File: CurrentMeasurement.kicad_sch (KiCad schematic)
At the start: 7 parts, among them U1 DDC112U

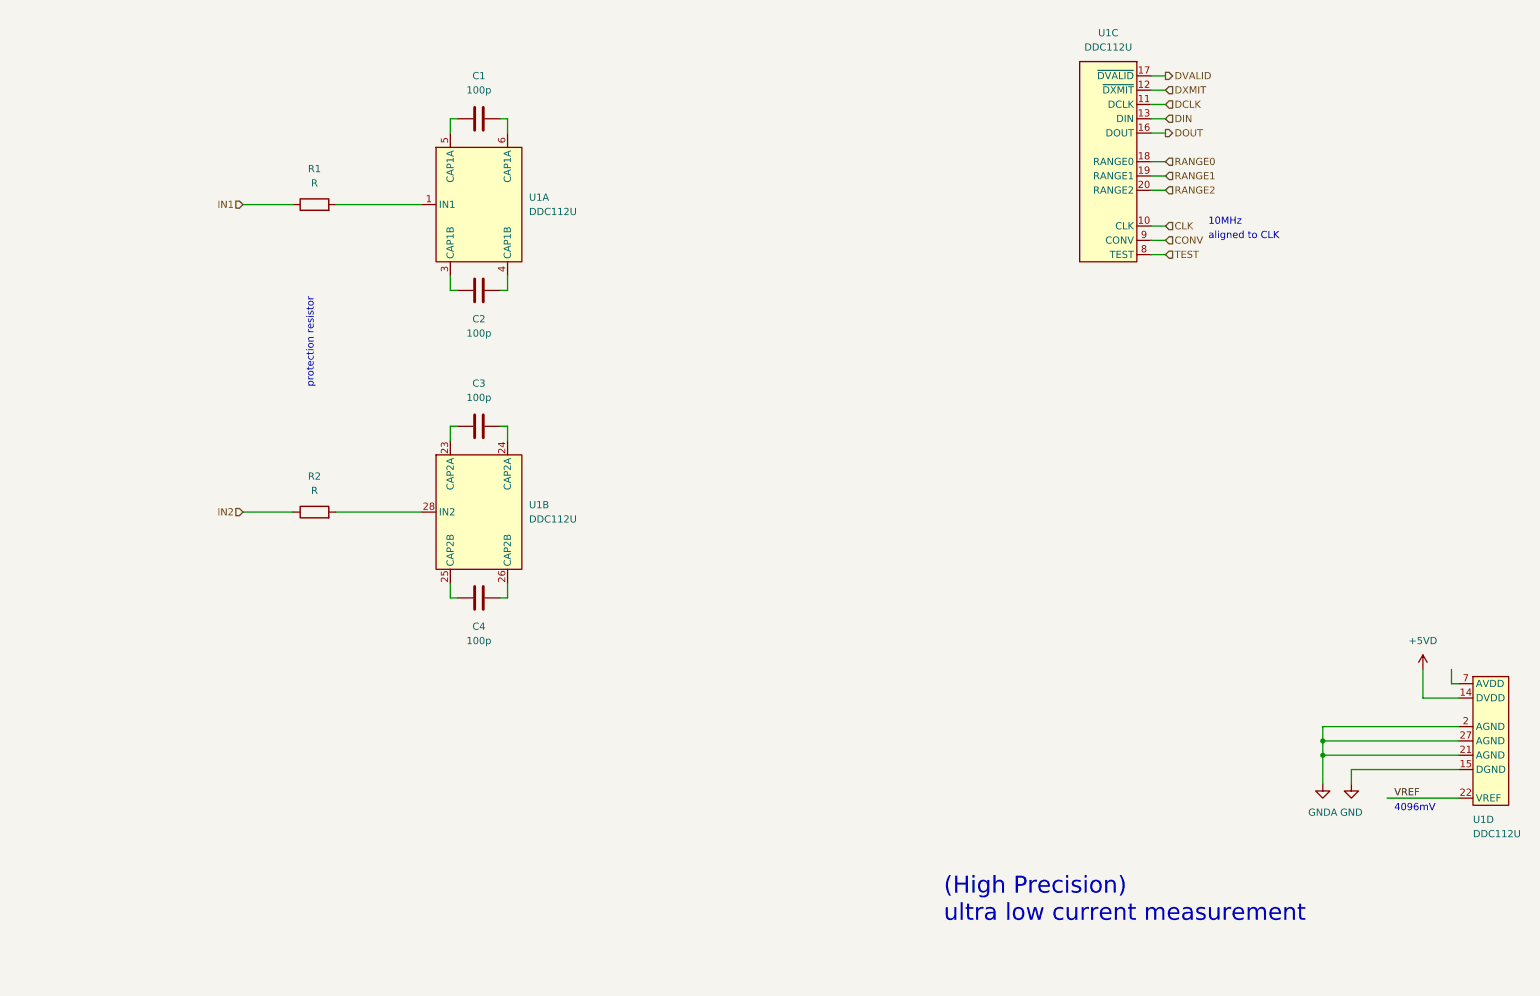
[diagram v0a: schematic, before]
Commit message: added decoupling Cs + reference voltage generation
for reference voltage generation, the buffer OPamp is missing
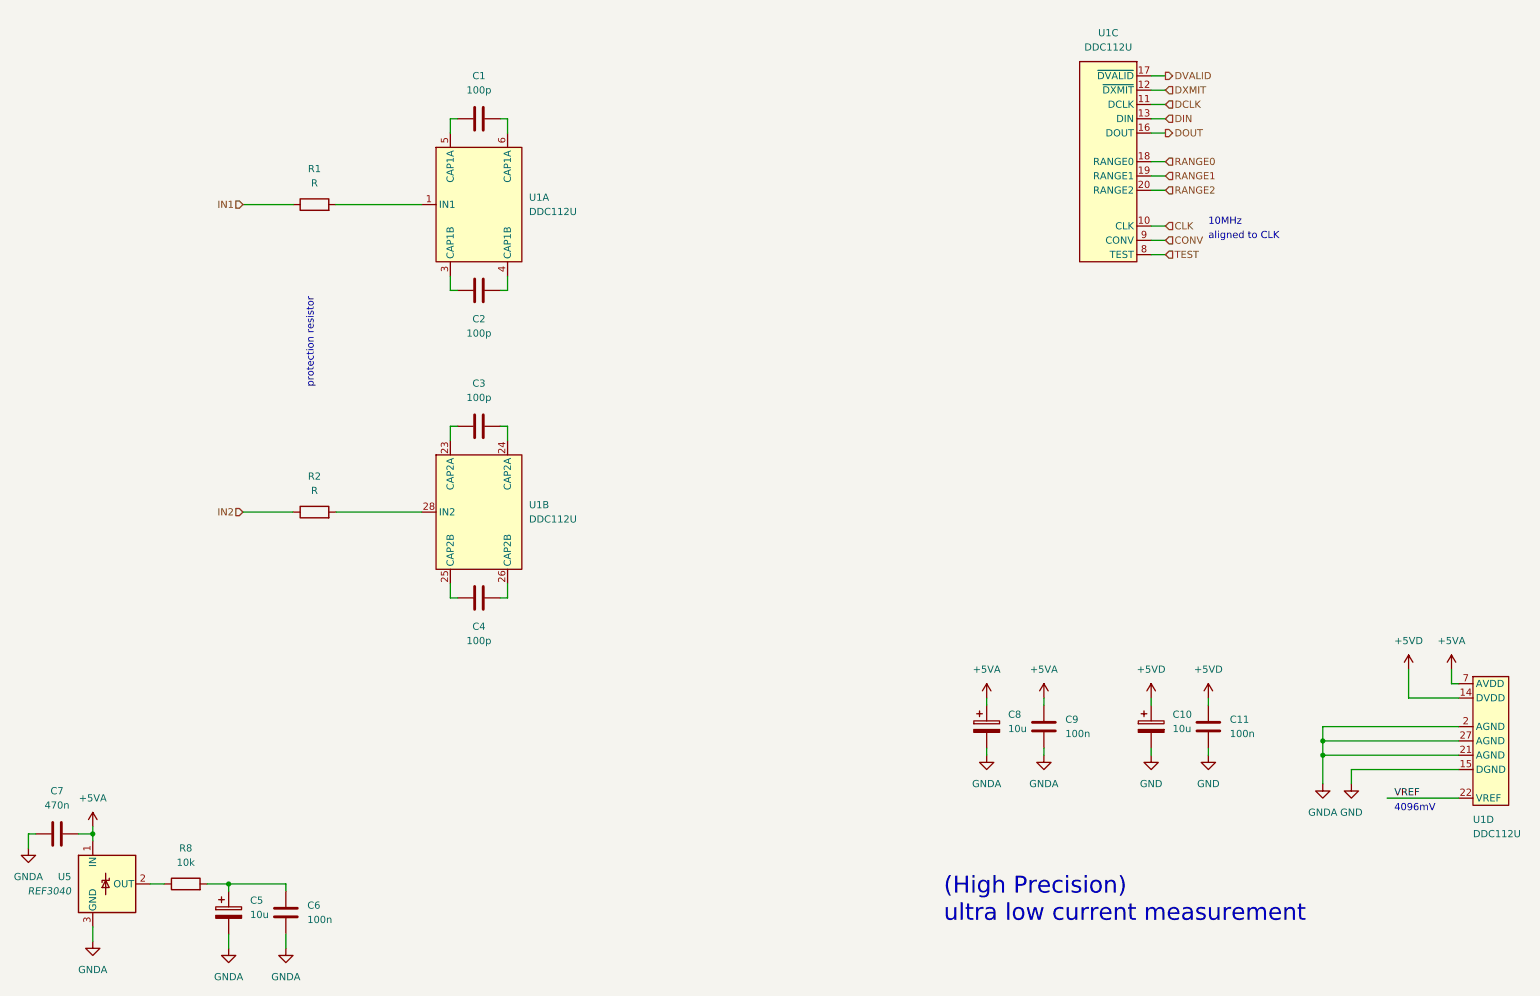
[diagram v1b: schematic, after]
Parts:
- added C10, C5, C8: 10u, Capacitor_SMD:CP_Elec_4x3.9, symbol Device:C_Polarized
- added C11, C6, C9: 100n, Capacitor_SMD:C_0603_1608Metric, symbol Device:C
- added C7: 470n, Capacitor_SMD:C_0603_1608Metric, symbol Device:C
- added R8: 10k, Resistor_SMD:R_0603_1608Metric, symbol Device:R
- added U5: REF3040, Package_TO_SOT_SMD:SOT-23, symbol Reference_Voltage:REF3040
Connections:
- net +5VD: now also C10.1, C11.1
- net GND: now also C10.2, C11.2
- net GNDA: now also C5.2, C6.2, C7.1, C8.2, C9.2, U5.3 (GND)
- net +5VA: now reaches U1.7 (AVDD)
- net +5VA: now also C7.2, C8.1, C9.1, U5.1 (IN)
- new net: C5.1, C6.1, R8.2
- new net: R8.1, U5.2 (OUT)

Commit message: changed title block to meaningful information
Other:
- title: (none) -> Open Nano Amp Meter
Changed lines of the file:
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@@
 (kicad_sch (version 20211123) (generator eeschema)
   (paper "A4")
+  (title_block
+    (title "Open Nano Amp Meter")
+    (date "2022-11-17")
+    (rev "0.9")
+  )
   (junction (at 246.38 146.05) (diameter 0) (color 0 0 0 0)
   )

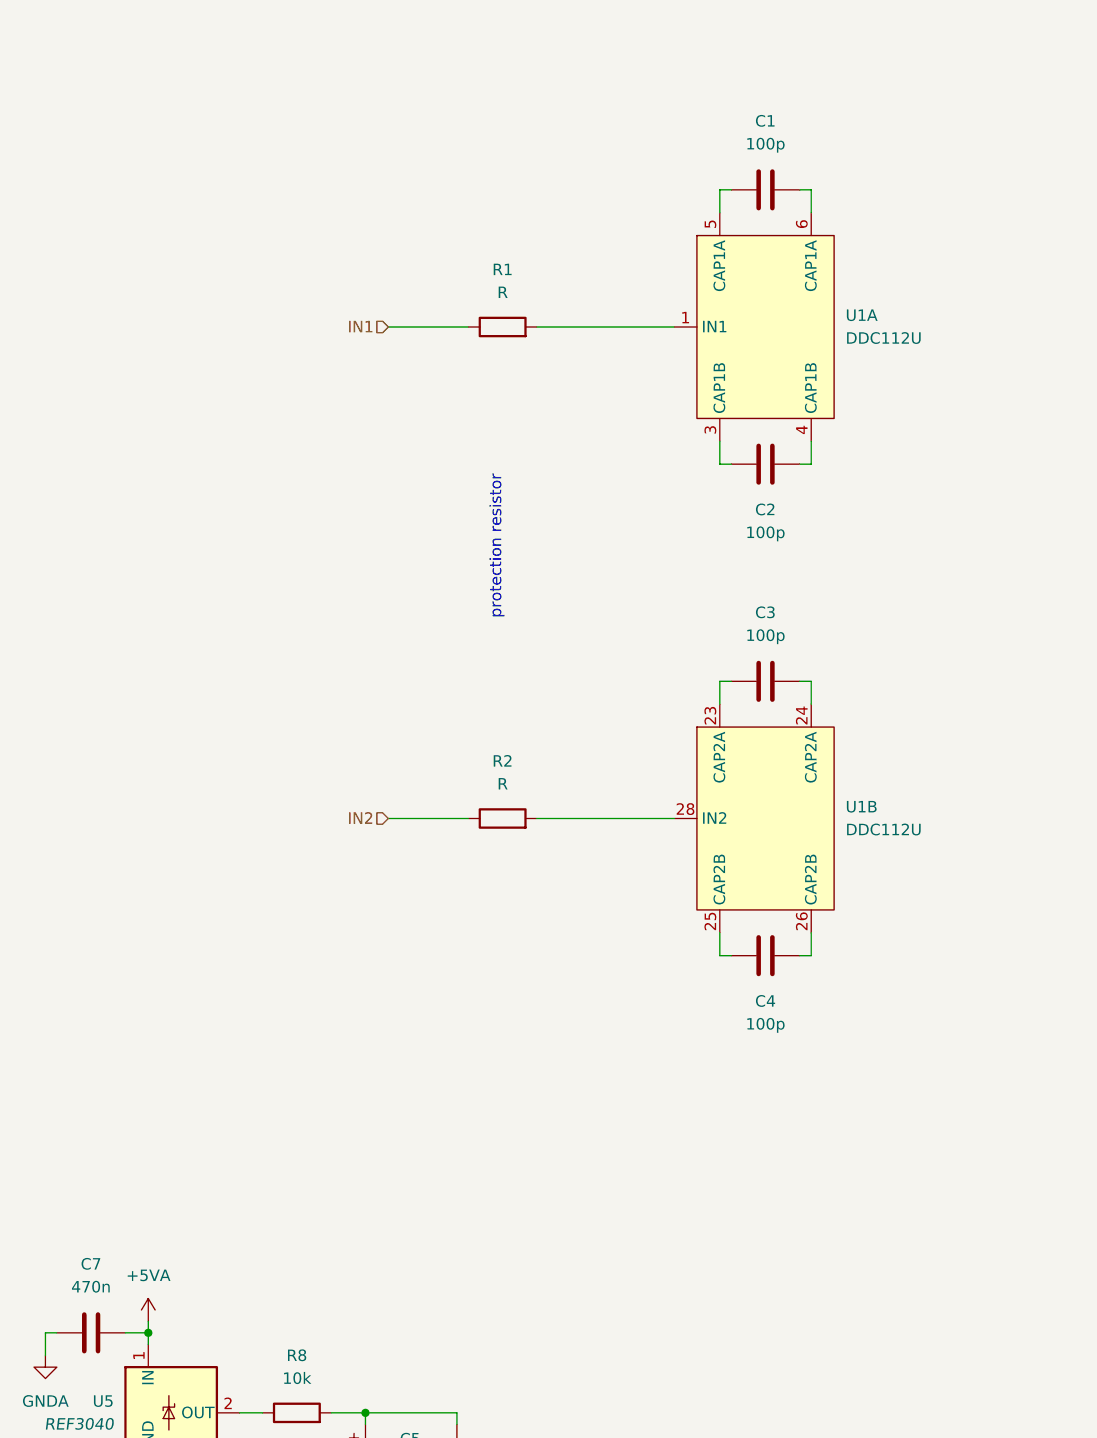
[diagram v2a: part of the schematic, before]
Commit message: added option to make the input bipolar
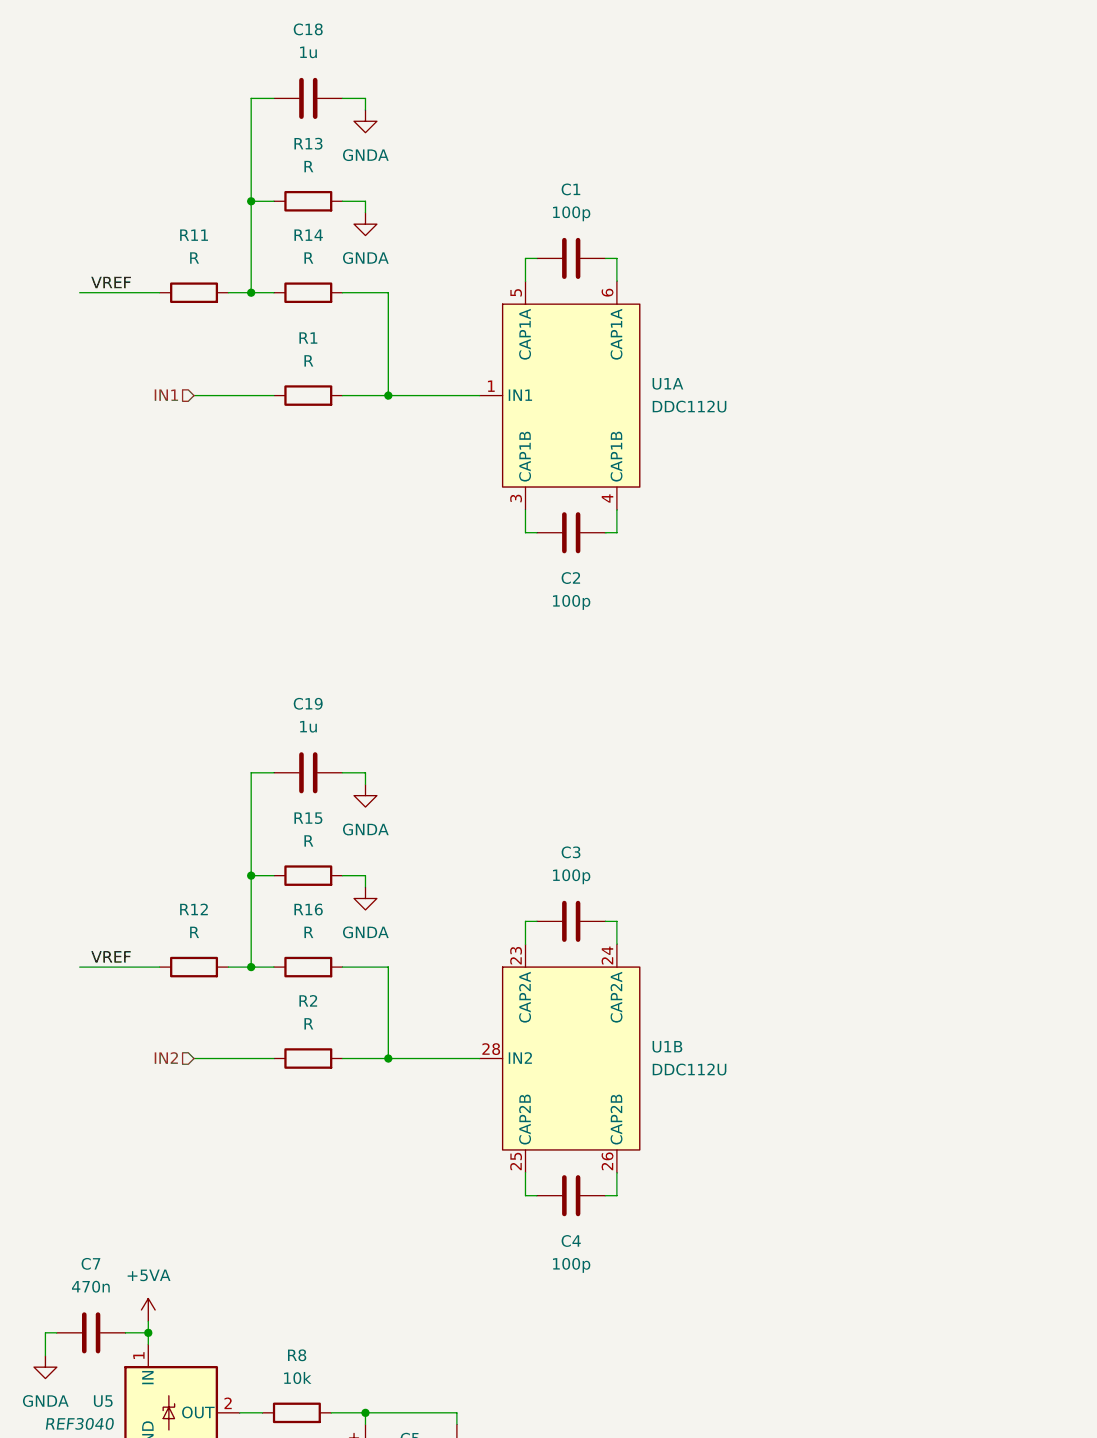
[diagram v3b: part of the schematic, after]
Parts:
- added C18, C19: 1u, Capacitor_SMD:C_0603_1608Metric, symbol Device:C
- added R11, R12, R13, R14, R15, R16: R, Resistor_SMD:R_0603_1608Metric, symbol Device:R
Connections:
- net GNDA: now also C18.2, C19.2, R13.2, R15.2
- net VREF: now also R11.1, R12.1
- net at R2.2, U1.28 (IN2): now also R16.2
- net at R1.2, U1.1 (IN1): now also R14.2
- new net: C18.1, R11.2, R13.1, R14.1
- new net: C19.1, R12.2, R15.1, R16.1
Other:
- note removed: "protection resistor"
- moved on the sheet: C1, C2, C3, C4, R1, R2, U1A, U1B
